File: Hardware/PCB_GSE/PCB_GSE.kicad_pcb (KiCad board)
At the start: 4 copper layers, 74 x 95.6 mm, 155 parts, among them J1 Conn_01x02, J2 BM03B-GHS-TBT, J3 GT17HN-4DP-2H(D)(56), J4 Conn_01x06_Pin, J5 Screw_Terminal_01x04, J6 Screw_Terminal_01x04, J7 Screw_Terminal_01x04, J8 Vin_XT30PW-F, U1 MAX6612MXK, U10 MP28167GQ-B-P, U2 ISOW1044, U3 SI5442DU-T1-GE3, U4 INA125UA/2K5, U5 STM32F103CBT6, U6 SI5442DU-T1-GE3, U7 SI5442DU-T1-GE3, U8 MPQ9843GLE-5-AEC1-Z, U9 TLV75733PDBVR, Y1 830050510

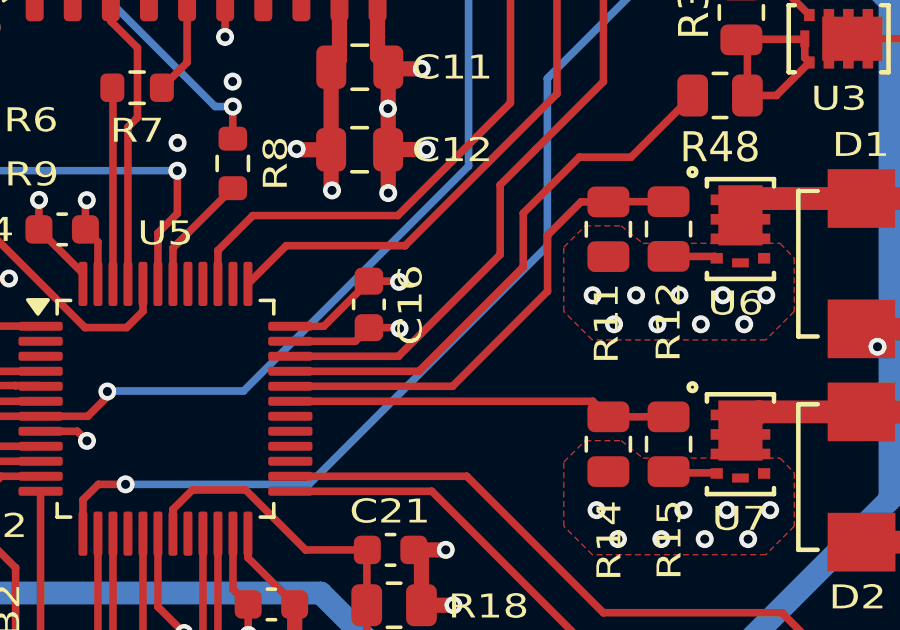
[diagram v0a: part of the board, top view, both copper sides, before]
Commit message: fix(gse): change Servo3_PWM -> TIM1_CH2, change Valve1/2_Open pin
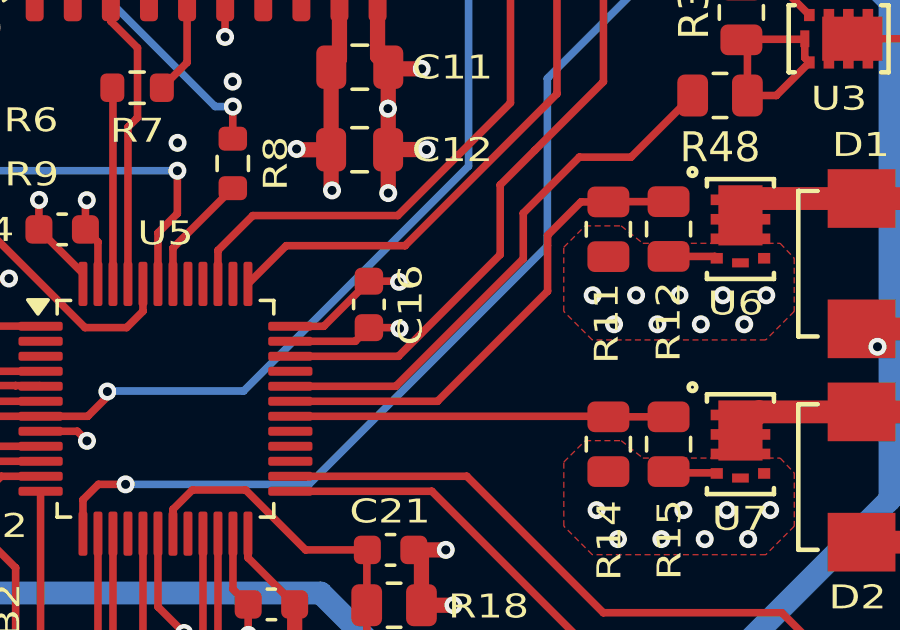
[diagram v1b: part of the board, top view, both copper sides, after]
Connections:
- net I2C2_SCL renamed 12V_I2C2_SCL
- net I2C2_SDA renamed 12V_I2C2_SDA
- U5 pad 30: unconnected-(U5-PA9-Pad30) -> Valve1_Open
- U5 pad 31: Valve1_Open -> Valve2_Open
- U5 pad 32: Valve2_Open -> Servo3_PWM
- U5 pad 33: Servo3_PWM -> unconnected-(U5-PA12-Pad33)
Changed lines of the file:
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@@
 	(net 38 "OSC_OUT")
 	(net 39 "Vin_Valve")
-	(net 40 "I2C2_SCL")
-	(net 41 "I2C2_SDA")
+	(net 40 "12V_I2C2_SCL")
+	(net 41 "12V_I2C2_SDA")
 	(net 42 "Power_Good_12V")
 	(net 43 "Power_Good_5V")
@@
 	(net 92 "unconnected-(U5-PA8-Pad29)")
 	(net 93 "unconnected-(U5-PB15-Pad28)")
-	(net 94 "unconnected-(U5-PA9-Pad30)")
+	(net 94 "unconnected-(U5-PA12-Pad33)")
 	(net 95 "unconnected-(U5-PC13-Pad2)")
 	(net 96 "unconnected-(U5-PB5-Pad41)")
@@
 			(layers "F.Cu" "F.Mask" "F.Paste")
 			(roundrect_rratio 0.25)
-			(net 40 "I2C2_SCL")
+			(net 40 "12V_I2C2_SCL")
 			(pinfunction "PB10")
 			(pintype "bidirectional")
@@
 			(layers "F.Cu" "F.Mask" "F.Paste")
 			(roundrect_rratio 0.25)
-			(net 41 "I2C2_SDA")
+			(net 41 "12V_I2C2_SDA")
 			(pinfunction "PB11")
 			(pintype "bidirectional")
@@
 			(layers "F.Cu" "F.Mask" "F.Paste")
 			(roundrect_rratio 0.25)
-			(net 94 "unconnected-(U5-PA9-Pad30)")
+			(net 34 "Valve1_Open")
 			(pinfunction "PA9")
-			(pintype "bidirectional+no_connect")
+			(pintype "bidirectional")
 		)
 		(pad "31" smd roundrect
@@
 			(layers "F.Cu" "F.Mask" "F.Paste")
 			(roundrect_rratio 0.25)
-			(net 34 "Valve1_Open")
+			(net 35 "Valve2_Open")
 			(pinfunction "PA10")
 			(pintype "bidirectional")
@@
 			(layers "F.Cu" "F.Mask" "F.Paste")
 			(roundrect_rratio 0.25)
-			(net 35 "Valve2_Open")
+			(net 71 "Servo3_PWM")
 			(pinfunction "PA11")
 			(pintype "bidirectional")
@@
 			(layers "F.Cu" "F.Mask" "F.Paste")
 			(roundrect_rratio 0.25)
-			(net 71 "Servo3_PWM")
+			(net 94 "unconnected-(U5-PA12-Pad33)")
 			(pinfunction "PA12")
-			(pintype "bidirectional")
+			(pintype "bidirectional+no_connect")
 		)
 		(pad "34" smd roundrect
@@
 			(size 0.7 0.25)
 			(layers "F.Cu" "F.Mask" "F.Paste")
-			(net 40 "I2C2_SCL")
+			(net 40 "12V_I2C2_SCL")
 			(pinfunction "SCL")
 			(pintype "unspecified")
@@
 			(size 1.2 0.25)
 			(layers "F.Cu" "F.Mask" "F.Paste")
-			(net 41 "I2C2_SDA")
+			(net 41 "12V_I2C2_SDA")
 			(pinfunction "SDA")
 			(pintype "unspecified")
@@
 			(layers "F.Cu" "F.Mask" "F.Paste")
 			(roundrect_rratio 0.243902)
-			(net 40 "I2C2_SCL")
+			(net 40 "12V_I2C2_SCL")
 			(pintype "passive")
 		)
@@
 			(layers "F.Cu" "F.Mask" "F.Paste")
 			(roundrect_rratio 0.243902)
-			(net 41 "I2C2_SDA")
+			(net 41 "12V_I2C2_SDA")
 			(pintype "passive")
 		)
@@
 	)
 	(segment
-		(start 168.024926 93.976619)
-		(end 168.012816 93.988729)
-		(width 0.254)
-		(layer "F.Cu")
-		(net 34)
-	)
-	(segment
-		(start 167.463463 93.478602)
+		(start 167.963463 93.978602)
 		(end 167.981715 93.996854)
 		(width 0.254)
@@
 	)
 	(segment
-		(start 157.380697 93.478602)
-		(end 167.463463 93.478602)
+		(start 157.380697 93.978602)
+		(end 167.963463 93.978602)
 		(width 0.254)
 		(layer "F.Cu")
@@
 	)
 	(segment
-		(start 165.95571 89.810276)
-		(end 165.95571 87.946257)
+		(start 157.380697 93.478602)
+		(end 162.287384 93.478602)
 		(width 0.254)
 		(layer "F.Cu")
@@
 	)
 	(segment
-		(start 167.069092 86.832875)
+		(start 167.98984 86.82475)
 		(end 167.981715 86.832875)
 		(width 0.254)
@@
 	)
 	(segment
-		(start 157.380697 92.978602)
-		(end 162.787384 92.978602)
+		(start 165.95571 89.810276)
+		(end 165.95571 87.946257)
 		(width 0.254)
 		(layer "F.Cu")
@@
 	)
 	(segment
-		(start 167.98984 86.82475)
-		(end 167.981715 86.832875)
+		(start 165.95571 87.946257)
+		(end 167.069092 86.832875)
 		(width 0.254)
 		(layer "F.Cu")
@@
 	)
 	(segment
-		(start 165.95571 87.946257)
-		(end 167.069092 86.832875)
+		(start 162.287384 93.478602)
+		(end 165.95571 89.810276)
 		(width 0.254)
 		(layer "F.Cu")
@@
 	)
 	(segment
-		(start 169.98825 86.82475)
-		(end 167.98984 86.82475)
+		(start 167.069092 86.832875)
+		(end 167.981715 86.832875)
 		(width 0.254)
 		(layer "F.Cu")
@@
 	)
 	(segment
-		(start 162.787384 92.978602)
-		(end 165.95571 89.810276)
+		(start 169.98825 86.82475)
+		(end 167.98984 86.82475)
 		(width 0.254)
 		(layer "F.Cu")
@@
 	)
 	(segment
-		(start 165.145267 88.999833)
-		(end 165.145267 87.208754)
+		(start 165.145267 87.208754)
+		(end 167.013036 85.340985)
 		(width 0.254)
 		(layer "F.Cu")
@@
 	)
 	(segment
-		(start 167.013036 85.340985)
-		(end 168.737115 85.340985)
+		(start 168.737115 85.340985)
+		(end 170.7915 83.2866)
 		(width 0.254)
 		(layer "F.Cu")
@@
 	)
 	(segment
-		(start 168.737115 85.340985)
-		(end 170.7915 83.2866)
+		(start 157.380697 92.978602)
+		(end 160.894398 92.978602)
 		(width 0.254)
 		(layer "F.Cu")
@@
 	)
 	(segment
-		(start 161.666498 92.478602)
-		(end 165.145267 88.999833)
+		(start 165.145267 88.727733)
+		(end 165.145267 87.208754)
 		(width 0.254)
 		(layer "F.Cu")
@@
 	)
 	(segment
-		(start 157.380697 92.478602)
-		(end 161.666498 92.478602)
+		(start 167.013036 85.340985)
+		(end 168.737115 85.340985)
 		(width 0.254)
 		(layer "F.Cu")
@@
 	)
 	(segment
-		(start 165.145267 87.208754)
-		(end 167.013036 85.340985)
+		(start 160.894398 92.978602)
+		(end 165.145267 88.727733)
 		(width 0.254)
 		(layer "F.Cu")

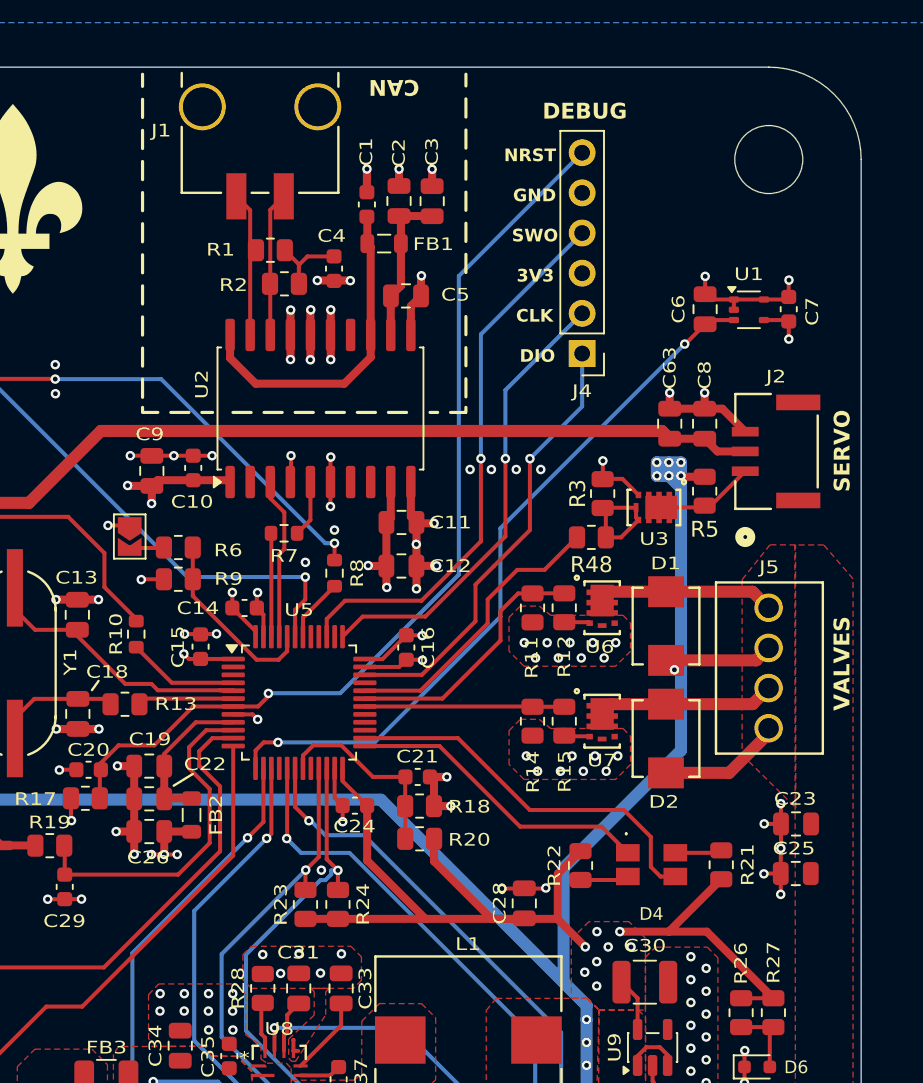
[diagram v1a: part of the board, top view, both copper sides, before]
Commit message: fix : cap electrolytique servo
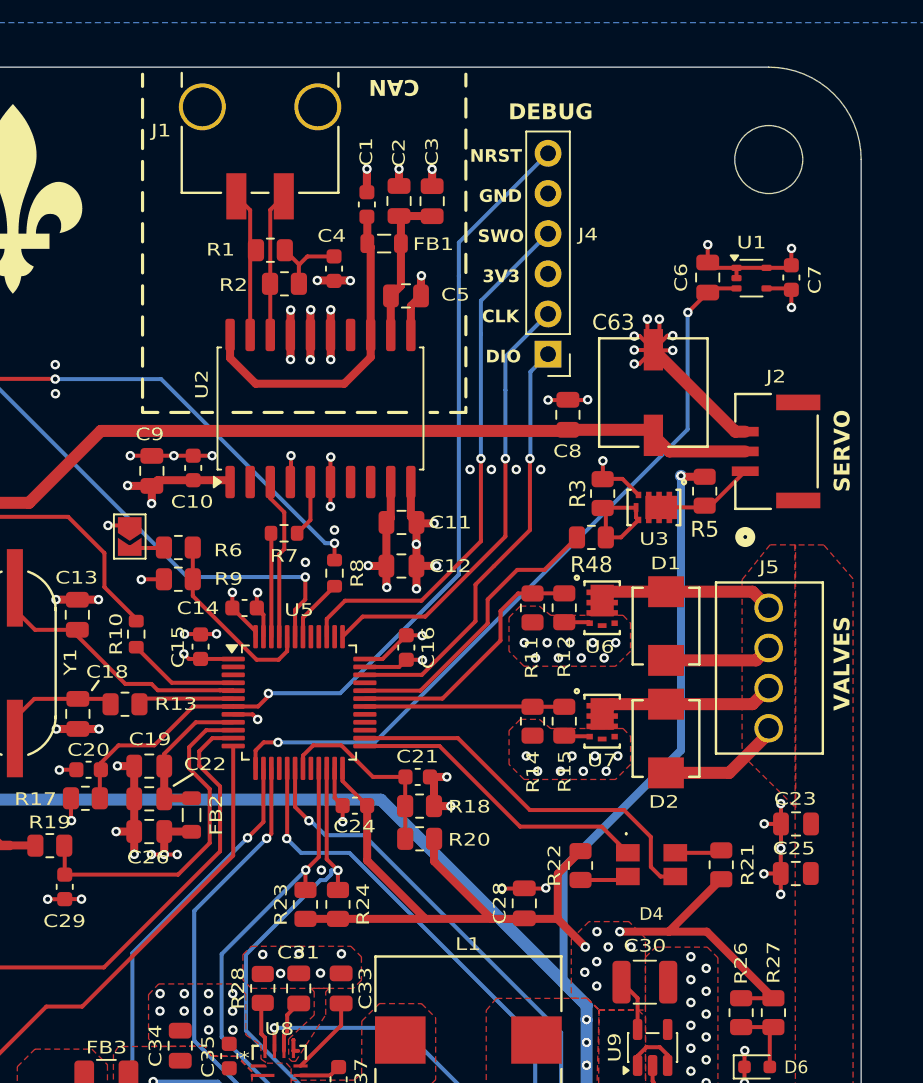
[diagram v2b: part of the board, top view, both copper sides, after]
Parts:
- C63: footprint Capacitor_SMD:C_0805_2012Metric -> PCB_GSE:U2-K_NCH
- moved C8 8.67 mm to (170.2, 75.5)
- moved G*** 3.50 mm to (154.9, 63.9)
- moved C63 2.23 mm to (175.6, 74.1)
- moved J4 2.16 mm to (169.0, 71.7)
- moved U1 2.01 mm to (181.8, 66.9)
- moved C7 2.01 mm to (184.3, 66.9)
- moved C6 2.01 mm to (179.1, 66.9)
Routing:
- net GND: track 131.6 -> 146.0 mm, vias 223 -> 229
- net 5V_Main: track 166.6 -> 159.9 mm, vias 20 -> 15
- net Temp_An: track 45.9 -> 48.0 mm
- net SYS_SWDIO: track 28.1 -> 27.2 mm
- net SYS_SWCLK: track 29.0 -> 28.1 mm
- net SYS_NRST: track 59.9 -> 58.9 mm
- net SYS_SWO: track 35.0 -> 34.1 mm

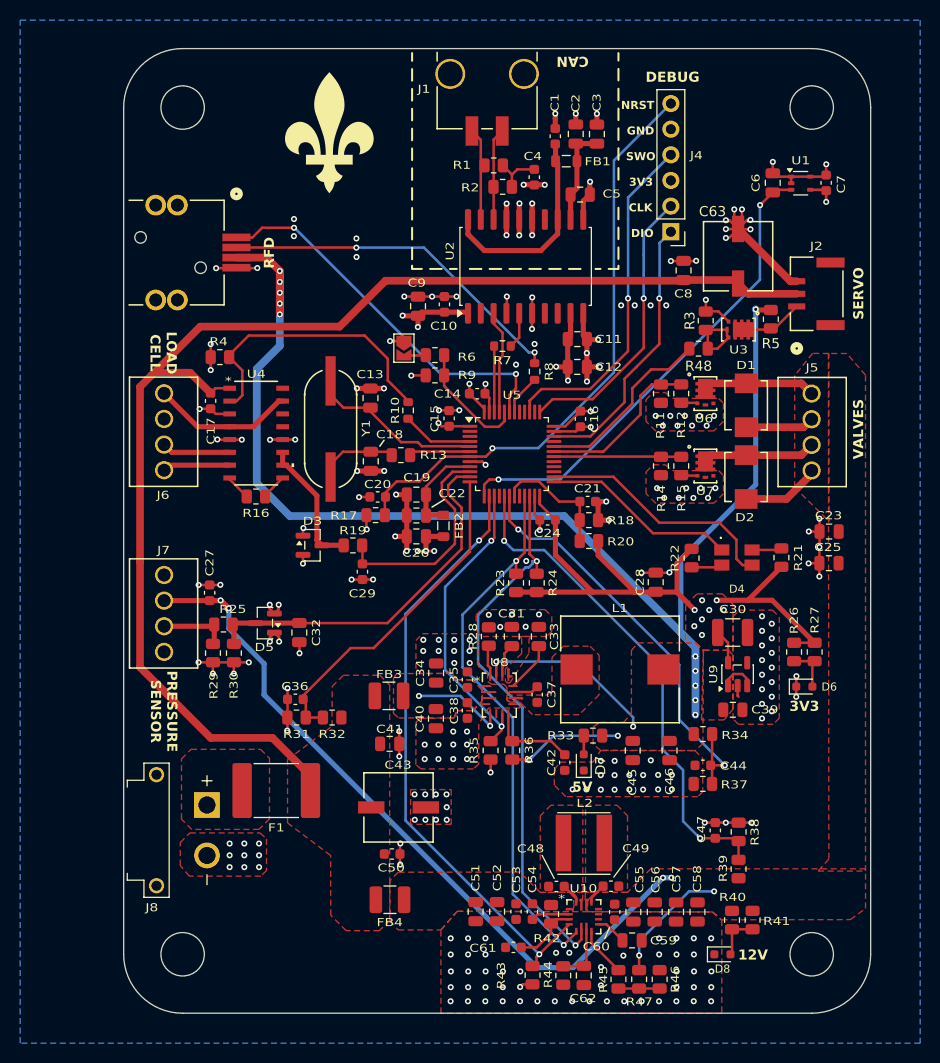
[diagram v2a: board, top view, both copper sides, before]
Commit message: fix: silkscreen green<->black + fix silkscreen + connect shield to gnd  in pressure sensor + fix/add doc
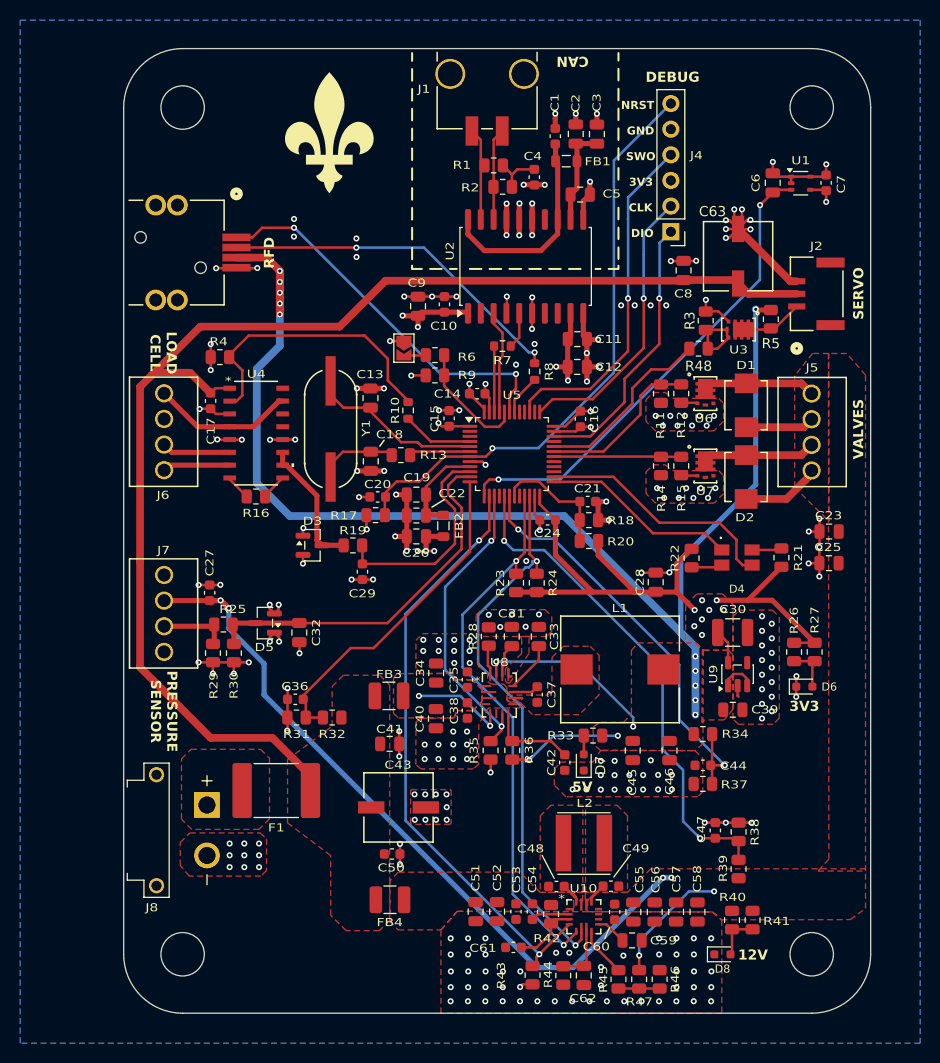
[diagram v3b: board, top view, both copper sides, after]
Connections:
- J7 pad 1: unconnected-(J7-Pin_1-Pad1) -> GND
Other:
- board text added: "GREY"
- board text added: "SHD"
- board text added: "Émile D'Amours-Sioui Samuel Gagnon Victor Deschênes Luka Dupuis Samuel Gauthier Oumou Kalssoum Cisse"
- board text removed: "GEEN"
- board text removed: "Émile D'Amours-Sioui Samuel Gagnon Victor Deschênes Luka Dupuis Samuel Gauthier"
